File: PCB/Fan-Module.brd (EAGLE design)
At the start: 58 x 66 mm, 27 parts, among them U1 ATSAMD11C14A-SSUT_ATSAMD11C14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, U3 LDL1117S12R_LDL1117S12R

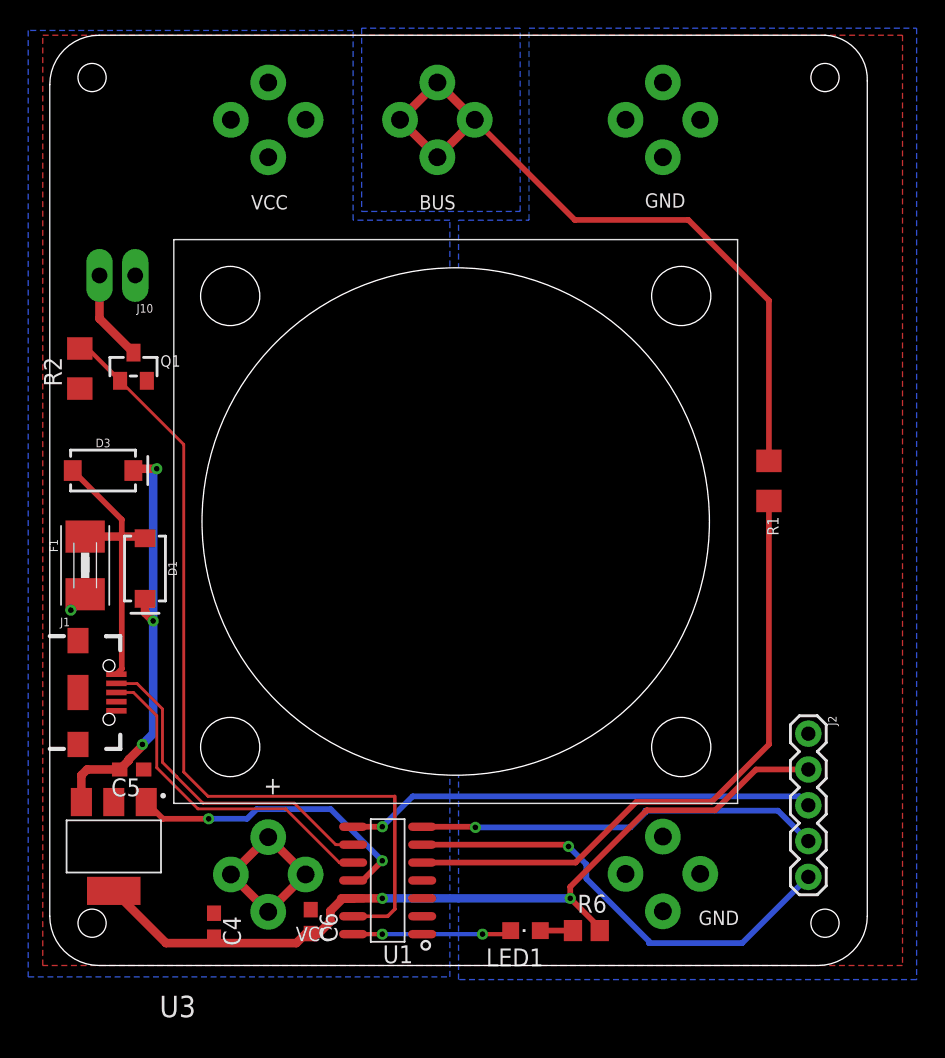
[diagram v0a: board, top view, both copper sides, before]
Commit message: added button to pcbs and did some fixing
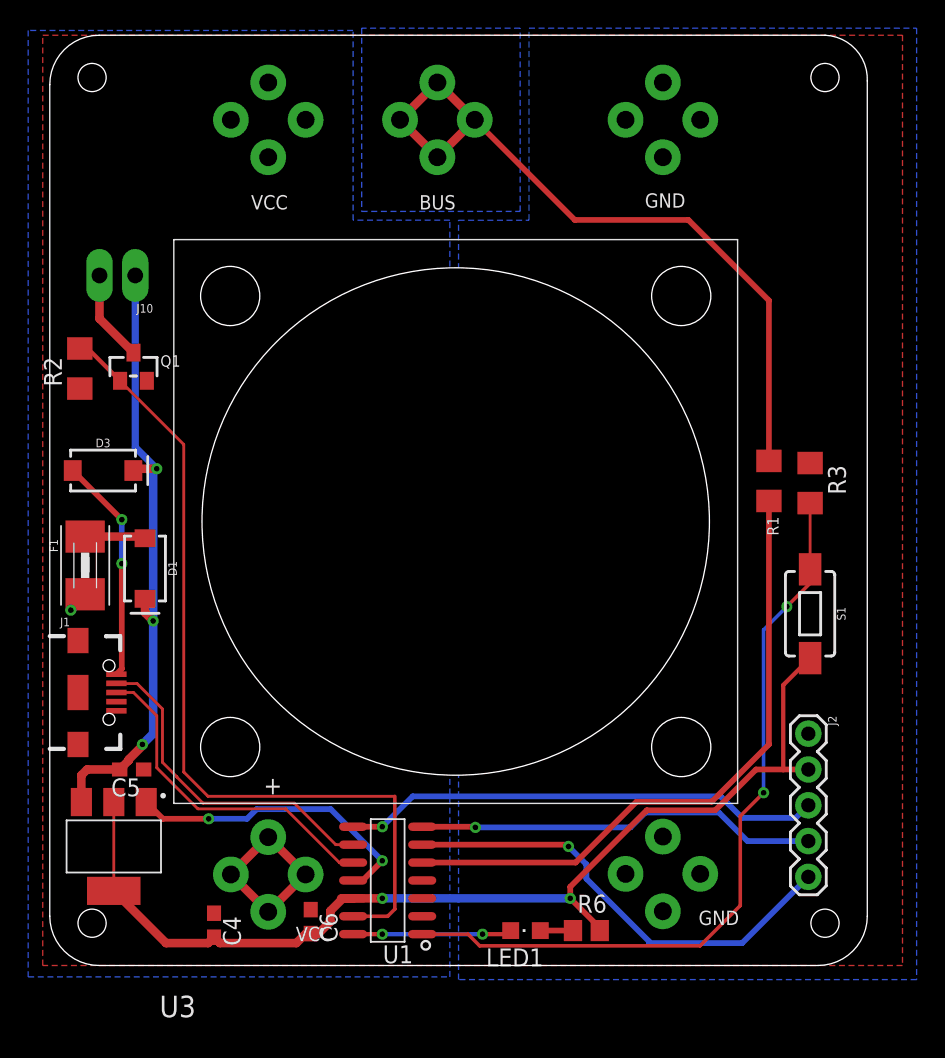
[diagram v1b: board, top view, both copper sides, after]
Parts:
- added R3: 2k, rcl:R1206
- added S1: MOMENTARY-SWITCH-SPST-SMD-6.0X3.5MM, SparkFun-Switches:TACTILE_SWITCH_SMD_6.0X3.5MM
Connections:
- new net N$7: R3.2, S1.1, U1.1
- net 3.3V: now also S1.2
- net GND: now also R3.1
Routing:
- net N$7: track 0.00 -> 54.7 mm, vias 0 -> 2
- net 3.3V: track 60.8 -> 76.2 mm
- net VCC: track 30.7 -> 45.1 mm
- net SWDIO: track 33.5 -> 34.2 mm
- net N$4: vias 0 -> 2

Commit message: added missing resistor before mosfet
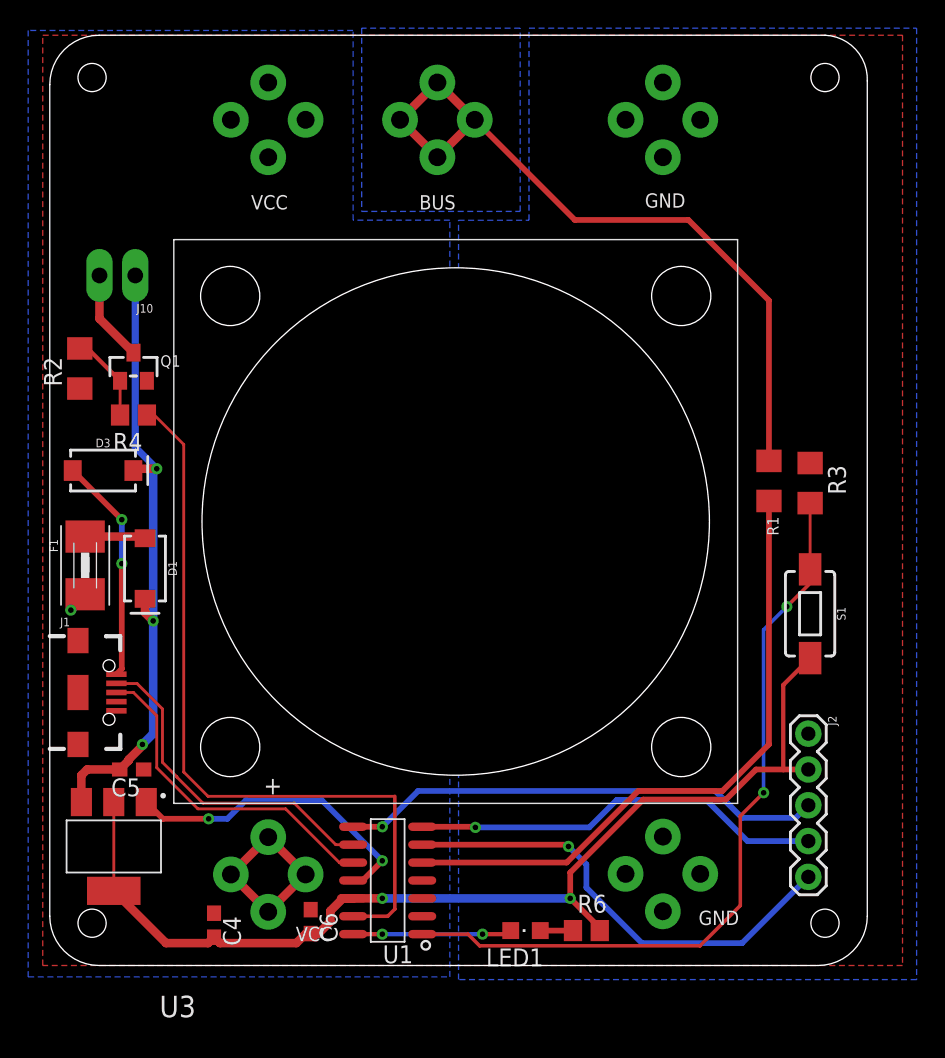
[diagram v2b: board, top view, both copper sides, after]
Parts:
- added R4: 499R, rcl:R0805
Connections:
- new net N$8: Q1.1, R2.2, R4.2
- net N$5: now also R4.1; no longer Q1.1, R2.2
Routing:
- net N$5: track 60.3 -> 53.6 mm
- net N$8: track 0.00 -> 6.24 mm
- net SWCLK: track 28.7 -> 29.4 mm
- net 3.3V: track 76.2 -> 76.8 mm
- net GND: track 22.0 -> 22.6 mm
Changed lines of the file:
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@@
 <?xml version="1.0" encoding="utf-8"?>
 <!DOCTYPE eagle SYSTEM "eagle.dtd">
-<eagle version="9.2.2">
+<eagle version="9.3.0">
 <drawing>
 <settings>
@@
 <attribute name="SF_SKU" value="COM-08229" x="59.944" y="28.956" size="1.778" layer="27" rot="R270" display="off"/>
 </element>
+<element name="R4" library="rcl" library_urn="urn:adsk.eagle:library:334" package="R0805" package3d_urn="urn:adsk.eagle:package:23553/2" value="499R" x="11.938" y="43.053" smashed="yes" rot="R180">
+<attribute name="NAME" x="12.573" y="41.783" size="1.27" layer="25" rot="R180"/>
+<attribute name="SPICEPREFIX" value="R" x="11.938" y="43.053" size="1.778" layer="27" rot="R180" display="off"/>
+<attribute name="VALUE" x="12.573" y="45.593" size="1.27" layer="27" rot="R180"/>
+</element>
 </elements>
 <signals>
@@
 <via x="17.272" y="14.40815" extent="1-16" drill="0.3937"/>
 <via x="29.591" y="11.43" extent="1-16" drill="0.3937"/>
-<wire x1="17.272" y1="14.40815" x2="19.99470625" y2="14.40815" width="0.4064" layer="16"/>
-<wire x1="19.99470625" y1="14.40815" x2="20.67675625" y2="15.0902" width="0.4064" layer="16"/>
-<wire x1="20.67675625" y1="15.0902" x2="25.9308" y2="15.0902" width="0.4064" layer="16"/>
-<wire x1="25.9308" y1="15.0902" x2="29.591" y2="11.43" width="0.4064" layer="16"/>
+<wire x1="17.272" y1="14.40815" x2="18.59770625" y2="14.40815" width="0.4064" layer="16"/>
+<wire x1="18.59770625" y1="14.40815" x2="19.91475625" y2="15.7252" width="0.4064" layer="16"/>
+<wire x1="19.91475625" y1="15.7252" x2="25.2958" y2="15.7252" width="0.4064" layer="16"/>
+<wire x1="25.2958" y1="15.7252" x2="29.591" y2="11.43" width="0.4064" layer="16"/>
 <wire x1="29.591" y1="11.43" x2="28.194" y2="10.033" width="0.4064" layer="1"/>
 <wire x1="28.194" y1="10.033" x2="27.522" y2="10.033" width="0.4064" layer="1"/>
@@
 <wire x1="42.926" y1="8.763" x2="45.019" y2="6.67" width="0.4064" layer="1"/>
 <wire x1="45.019" y1="6.67" x2="45.019" y2="6.477" width="0.4064" layer="1"/>
-<wire x1="48.35560625" y1="15.0114" x2="42.926" y2="9.58179375" width="0.4064" layer="1"/>
-<wire x1="42.926" y1="8.763" x2="42.926" y2="9.58179375" width="0.4064" layer="1"/>
+<wire x1="48.10160625" y1="15.7734" x2="42.926" y2="10.59779375" width="0.4064" layer="1"/>
+<wire x1="42.926" y1="8.763" x2="42.926" y2="10.59779375" width="0.4064" layer="1"/>
 <wire x1="56.10710625" y1="17.907" x2="58.039" y2="17.907" width="0.4064" layer="1"/>
 <wire x1="58.039" y1="17.907" x2="59.817" y2="17.907" width="0.4064" layer="1"/>
-<wire x1="53.21150625" y1="15.0114" x2="56.10710625" y2="17.907" width="0.4064" layer="1"/>
-<wire x1="48.35560625" y1="15.0114" x2="53.21150625" y2="15.0114" width="0.4064" layer="1"/>
+<wire x1="53.97350625" y1="15.7734" x2="56.10710625" y2="17.907" width="0.4064" layer="1"/>
+<wire x1="48.10160625" y1="15.7734" x2="53.97350625" y2="15.7734" width="0.4064" layer="1"/>
 <wire x1="24.169" y1="6.262" x2="23.495" y2="5.588" width="0.6096" layer="1"/>
 <wire x1="24.169" y1="6.262" x2="24.511" y2="6.262" width="0.6096" layer="1"/>
@@
 <via x="42.799" y="12.446" extent="1-16" drill="0.3937"/>
 <wire x1="42.799" y1="12.446" x2="44.069" y2="11.176" width="0.4064" layer="16"/>
-<wire x1="44.069" y1="11.176" x2="44.069" y2="10.16" width="0.4064" layer="16"/>
-<wire x1="44.069" y1="10.16" x2="48.514" y2="5.715" width="0.4064" layer="16"/>
-<wire x1="48.514" y1="5.715" x2="48.514" y2="5.588" width="0.4064" layer="16"/>
-<wire x1="48.514" y1="5.588" x2="55.118" y2="5.588" width="0.4064" layer="16"/>
+<wire x1="44.069" y1="11.176" x2="44.069" y2="9.525" width="0.4064" layer="16"/>
+<wire x1="44.069" y1="9.525" x2="48.006" y2="5.588" width="0.4064" layer="16"/>
+<wire x1="48.006" y1="5.588" x2="55.118" y2="5.588" width="0.4064" layer="16"/>
 <wire x1="55.118" y1="5.588" x2="59.817" y2="10.287" width="0.4064" layer="16"/>
 </signal>
@@
 <wire x1="36.15055" y1="13.843" x2="36.195" y2="13.79855" width="0.4064" layer="1"/>
 <via x="36.195" y="13.79855" extent="1-16" drill="0.3937"/>
-<wire x1="36.195" y1="13.79855" x2="47.19955" y2="13.79855" width="0.4064" layer="16"/>
-<wire x1="48.26" y1="14.859" x2="53.467" y2="14.859" width="0.4064" layer="16"/>
+<wire x1="36.195" y1="13.79855" x2="44.27855" y2="13.79855" width="0.4064" layer="16"/>
+<wire x1="46.228" y1="15.748" x2="52.578" y2="15.748" width="0.4064" layer="16"/>
 <wire x1="55.499" y1="12.827" x2="59.817" y2="12.827" width="0.4064" layer="16"/>
-<wire x1="55.499" y1="12.827" x2="53.467" y2="14.859" width="0.4064" layer="16"/>
-<wire x1="47.19955" y1="13.79855" x2="48.26" y2="14.859" width="0.4064" layer="16"/>
+<wire x1="55.499" y1="12.827" x2="52.578" y2="15.748" width="0.4064" layer="16"/>
+<wire x1="44.27855" y1="13.79855" x2="46.228" y2="15.748" width="0.4064" layer="16"/>
 </signal>
 <signal name="SWDIO">
@@
 <wire x1="27.522" y1="13.843" x2="29.591" y2="13.843" width="0.4064" layer="1"/>
 <via x="29.591" y="13.843" extent="1-16" drill="0.3937"/>
-<wire x1="29.591" y1="13.843" x2="31.75" y2="16.002" width="0.4064" layer="16"/>
-<wire x1="53.594" y1="16.002" x2="55.118" y2="14.478" width="0.4064" layer="16"/>
+<wire x1="29.591" y1="13.843" x2="32.131" y2="16.383" width="0.4064" layer="16"/>
+<wire x1="53.213" y1="16.383" x2="55.118" y2="14.478" width="0.4064" layer="16"/>
 <wire x1="55.118" y1="14.478" x2="58.928" y2="14.478" width="0.4064" layer="16"/>
 <wire x1="58.928" y1="14.478" x2="59.817" y2="15.367" width="0.4064" layer="16"/>
-<wire x1="31.75" y1="16.002" x2="53.594" y2="16.002" width="0.4064" layer="16"/>
+<wire x1="32.131" y1="16.383" x2="53.213" y2="16.383" width="0.4064" layer="16"/>
 </signal>
 <signal name="N$4">
@@
 </signal>
 <signal name="N$5">
-<contactref element="Q1" pad="1"/>
-<contactref element="R2" pad="2"/>
 <contactref element="U1" pad="13"/>
-<wire x1="8.128" y1="47.777" x2="8.693" y2="47.777" width="0.3048" layer="1"/>
-<wire x1="8.693" y1="47.777" x2="10.988" y2="45.482" width="0.3048" layer="1"/>
 <wire x1="30.48" y1="16.002" x2="30.48" y2="8.001" width="0.254" layer="1"/>
 <wire x1="30.48" y1="8.001" x2="29.972" y2="7.493" width="0.254" layer="1"/>
 <wire x1="29.972" y1="7.493" x2="27.522" y2="7.493" width="0.254" layer="1"/>
-<wire x1="10.988" y1="45.482" x2="15.5046" y2="40.9654" width="0.2032" layer="1"/>
-<wire x1="15.5046" y1="40.9654" x2="15.5046" y2="17.7268125" width="0.2032" layer="1"/>
+<wire x1="15.5046" y1="17.7268125" x2="15.5046" y2="40.9654" width="0.2032" layer="1"/>
 <wire x1="15.5046" y1="17.7268125" x2="17.2294125" y2="16.002" width="0.2032" layer="1"/>
 <wire x1="17.2294125" y1="16.002" x2="30.48" y2="16.002" width="0.2032" layer="1"/>
+<contactref element="R4" pad="1"/>
+<wire x1="15.5046" y1="40.9654" x2="13.417" y2="43.053" width="0.2032" layer="1"/>
+<wire x1="13.417" y1="43.053" x2="12.888" y2="43.053" width="0.2032" layer="1"/>
 </signal>
 <signal name="FAN">
@@
 <contactref element="R1" pad="2"/>
 <contactref element="U1" pad="5"/>
-<wire x1="32.422" y1="11.303" x2="43.307" y2="11.303" width="0.4064" layer="1"/>
-<wire x1="43.307" y1="11.303" x2="47.625" y2="15.621" width="0.4064" layer="1"/>
-<wire x1="47.625" y1="15.621" x2="52.959" y2="15.621" width="0.4064" layer="1"/>
-<wire x1="52.959" y1="15.621" x2="57.023" y2="19.685" width="0.4064" layer="1"/>
+<wire x1="32.422" y1="11.303" x2="42.672" y2="11.303" width="0.4064" layer="1"/>
+<wire x1="42.672" y1="11.303" x2="47.752" y2="16.383" width="0.4064" layer="1"/>
+<wire x1="47.752" y1="16.383" x2="53.721" y2="16.383" width="0.4064" layer="1"/>
+<wire x1="53.721" y1="16.383" x2="57.023" y2="19.685" width="0.4064" layer="1"/>
 <wire x1="57.023" y1="19.685" x2="57.023" y2="36.957" width="0.4064" layer="1"/>
 </signal>
@@
 <wire x1="54.991" y1="8.255" x2="52.1328" y2="5.3968" width="0.254" layer="1"/>
 </signal>
+<signal name="N$8">
+<contactref element="Q1" pad="1"/>
+<contactref element="R2" pad="2"/>
+<contactref element="R4" pad="2"/>
+<wire x1="8.128" y1="47.777" x2="8.693" y2="47.777" width="0.3048" layer="1"/>
+<wire x1="8.693" y1="47.777" x2="10.988" y2="45.482" width="0.3048" layer="1"/>
+<wire x1="10.988" y1="43.053" x2="10.988" y2="45.482" width="0.2032" layer="1"/>
+</signal>
 </signals>

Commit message: removed buttons.. not needed
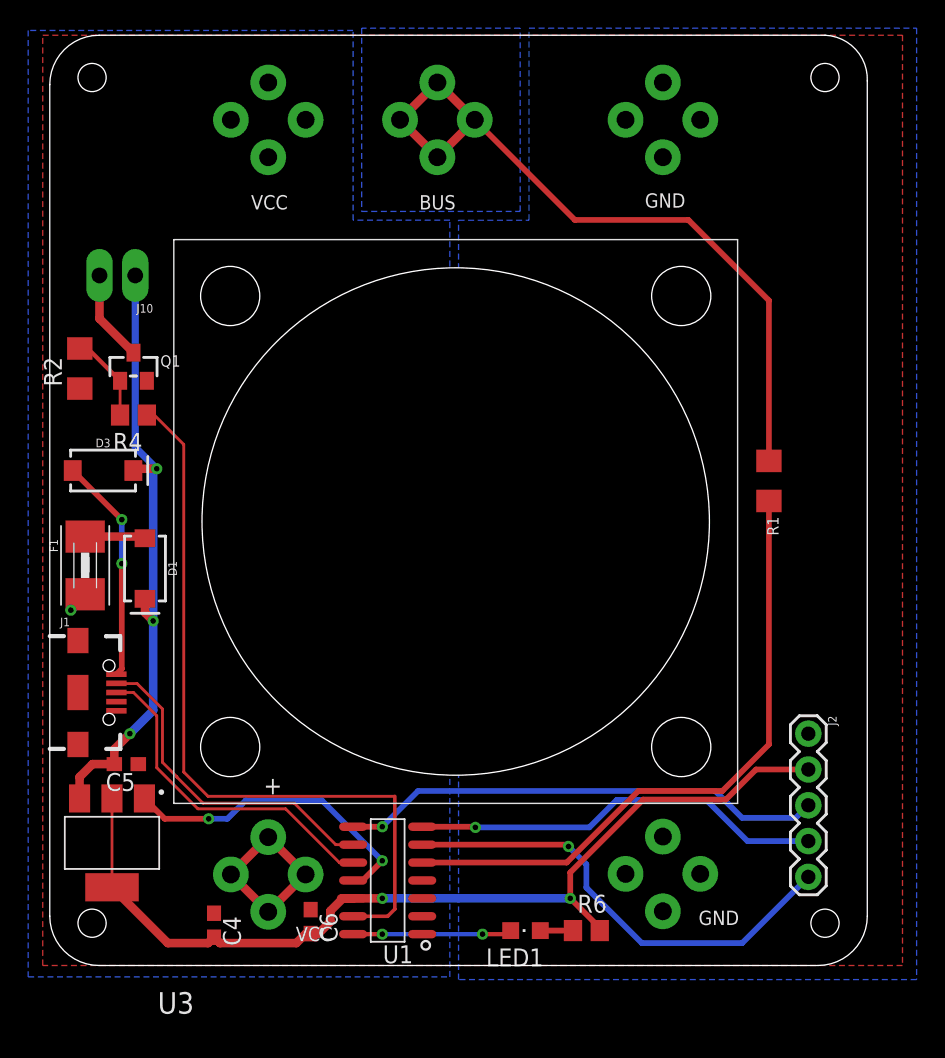
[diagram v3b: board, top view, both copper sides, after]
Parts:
- removed R3: 2k, rcl:R1206
- removed S1: MOMENTARY-SWITCH-SPST-SMD-6.0X3.5MM, SparkFun-Switches:TACTILE_SWITCH_SMD_6.0X3.5MM
- moved C5 0.54 mm to (11.4, 18.3)
- moved U3 0.28 mm to (10.4, 12.7)
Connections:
- removed net N$7: R3.2, S1.1, U1.1
- net 3.3V: no longer S1.2
- net GND: no longer R3.1
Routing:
- net N$7: track 54.7 -> 0.00 mm, vias 2 -> 0
- net 3.3V: track 76.8 -> 68.3 mm
- net VCC: track 45.1 -> 44.4 mm
